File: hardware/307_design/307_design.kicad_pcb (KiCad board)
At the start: 2 copper layers, 80 x 54.5 mm, 45 parts, among them J1 USB_B_Micro, J10 Conn_01x04, J11 Conn_02x05_Top_Bottom, J12 Conn_01x04, J2 Conn_01x03, J3 Conn_01x04, J4 Conn_02x03_Odd_Even, J5 Conn_02x03_Odd_Even, J6 Conn_01x04, J7 Conn_02x03_Odd_Even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

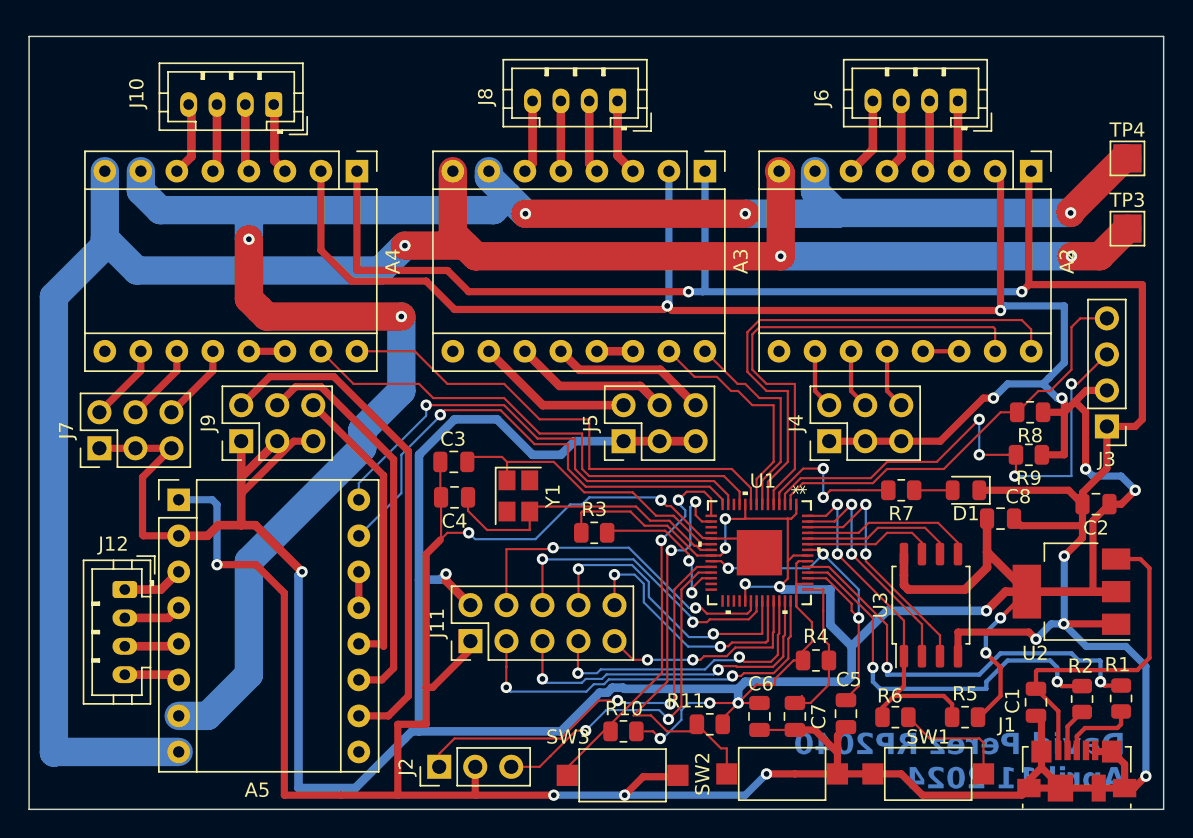
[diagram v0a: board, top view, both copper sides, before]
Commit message: update traces and add sample program
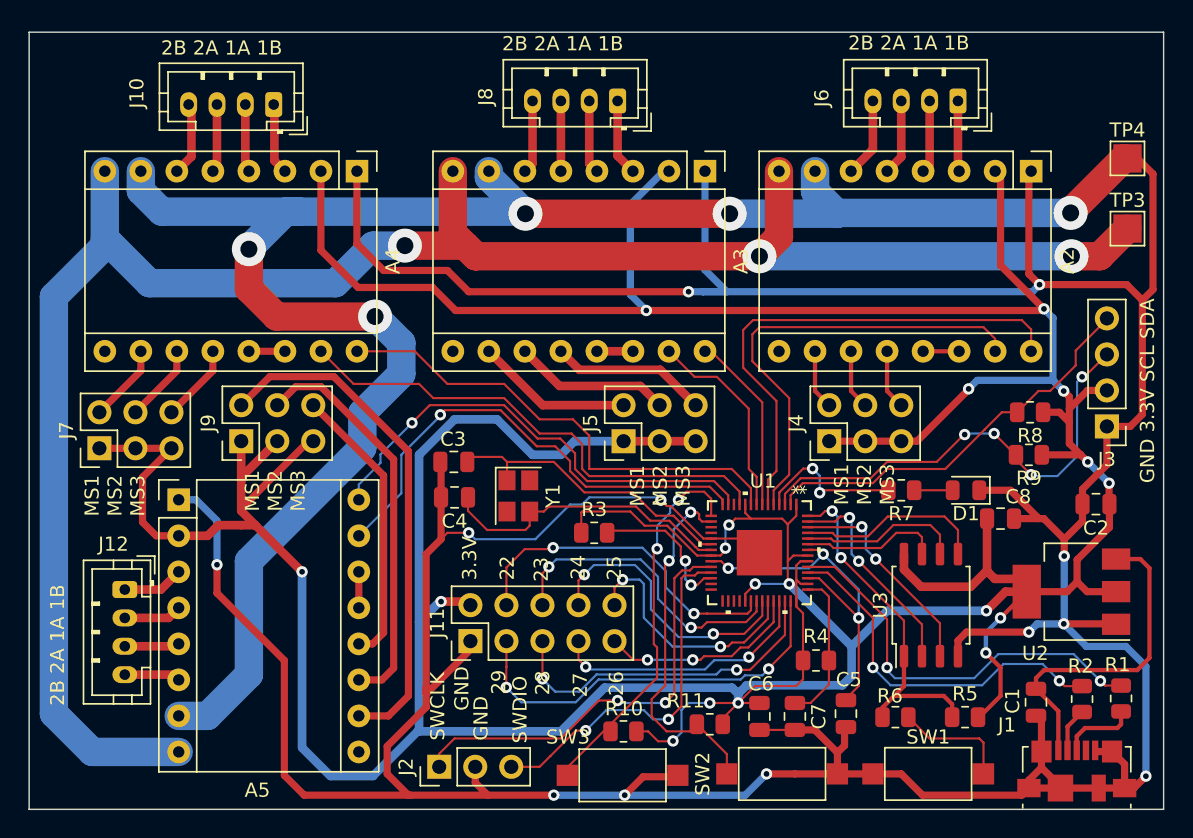
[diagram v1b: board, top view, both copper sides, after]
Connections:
- A2 pad 1: GND -> TP_GND
- A3 pad 1: GND -> TP_GND
- A4 pad 1: GND -> TP_GND
- A5 pad 1: GND -> TP_GND
- C1 pad 2: GND -> TP_GND
- C2 pad 2: GND -> TP_GND
- C3 pad 2: GND -> TP_GND
- C4 pad 2: GND -> TP_GND
- C5 pad 2: GND -> TP_GND
- C6 pad 2: GND -> TP_GND
- C7 pad 2: GND -> TP_GND
- C8 pad 2: GND -> TP_GND
- D1 pad 1: GND -> TP_GND
- J1 pad 5: GND -> TP_GND
- J1 pad 6: GND -> TP_GND
- J11 pad 1: GND -> TP_GND
- J2 pad 2: GND -> TP_GND
- J3 pad 1: GND -> TP_GND
- SW1 pad 1: GND -> TP_GND
- SW2 pad 2: GND -> TP_GND
- SW3 pad 2: GND -> TP_GND
- U1 pad 19: GND -> TP_GND
- U1 pad 57: GND -> TP_GND
- U2 pad 1: GND -> TP_GND
- U3 pad 4: GND -> TP_GND
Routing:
- net TP_GND: track 133.4 -> 462.5 mm, vias 5 -> 17
- net GND: track 322.0 -> 0.00 mm, vias 12 -> 0
- net +3.3V: track 397.7 -> 387.9 mm
- net SCL: track 37.7 -> 33.3 mm
- net BUTTON1: track 29.4 -> 25.6 mm
- net IO2: track 17.6 -> 15.2 mm
- net GPIO27: track 21.0 -> 18.8 mm
- net M2_STEP: track 16.5 -> 14.3 mm
- net M2_DIR: track 14.7 -> 12.7 mm
- net M1_STEP: track 34.0 -> 32.1 mm
- net USB_DM: track 27.8 -> 26.0 mm
- net IO1: track 16.3 -> 15.0 mm
- net IO0: track 12.3 -> 13.4 mm
- net SDA: track 29.9 -> 28.8 mm
- net GPIO25: track 18.8 -> 17.7 mm
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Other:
- board size 80 x 54.5 mm -> 80 x 54.8 mm
- board text added: "29"
- board text added: "2B 2A 1A 1B"
- board text added: "GND 3.3V SCL SDA"
- board text added: "MS1 MS2 MS3"
- board text removed: "1A"
- board text removed: "1B"
- board text removed: "2A"
- board text removed: "2B"
- board text removed: "30"
- board text removed: "MS1"
- board text removed: "MS2"
- board text removed: "MS3"
- board text removed: "SCL"
- board text removed: "SDA"
